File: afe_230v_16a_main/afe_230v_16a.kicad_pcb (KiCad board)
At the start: 2 copper layers, 146 x 86.4 mm, 69 parts, among them J1 MKDSN 2,5/ 6-5,08, J2 MKDS 1,5/ 6, J5 HBUS16, J6 pinheader_2x6_socket, J9 Conn_01x04_STlink_pinheader, U10 BlackPill_F4_SWI, U2 AD8538, U3 AD8538_dnp, U4 AQH3223A, U5 ACS711xLCTR-25AB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

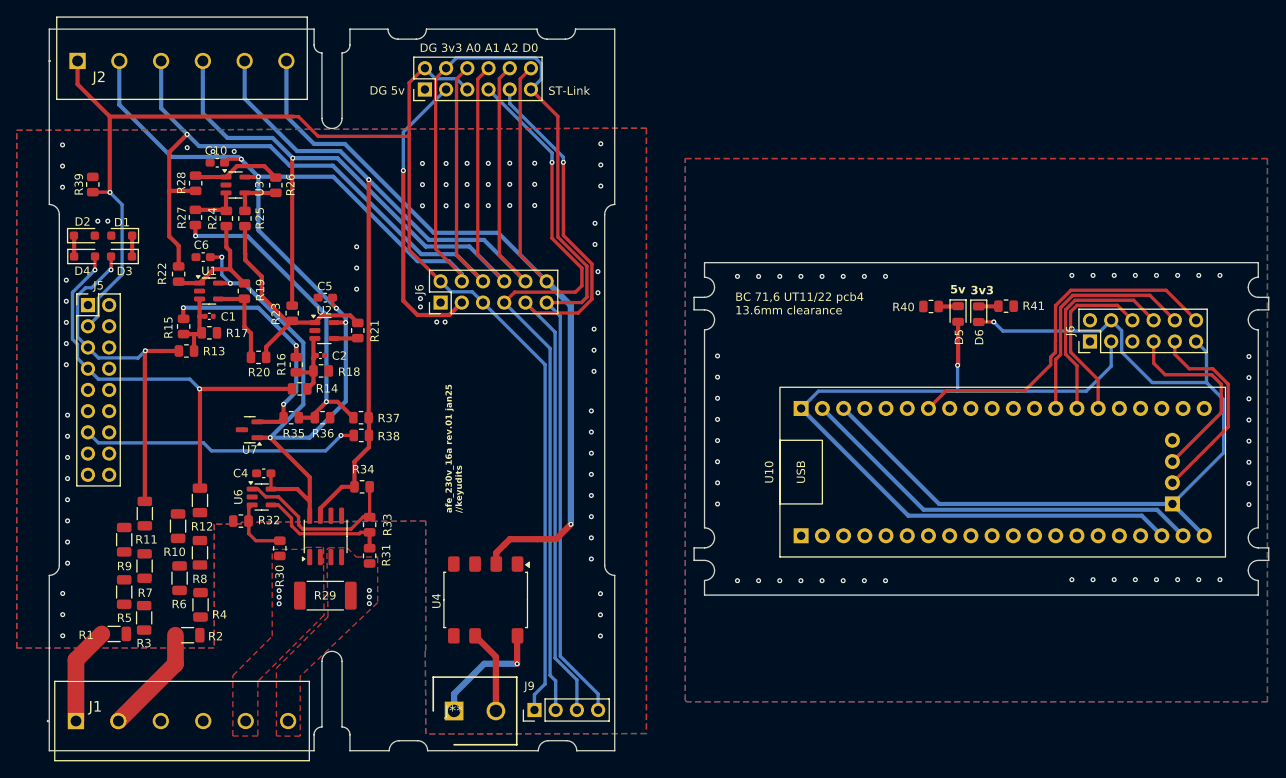
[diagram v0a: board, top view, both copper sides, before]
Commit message: added 15/16 0ohm resistors
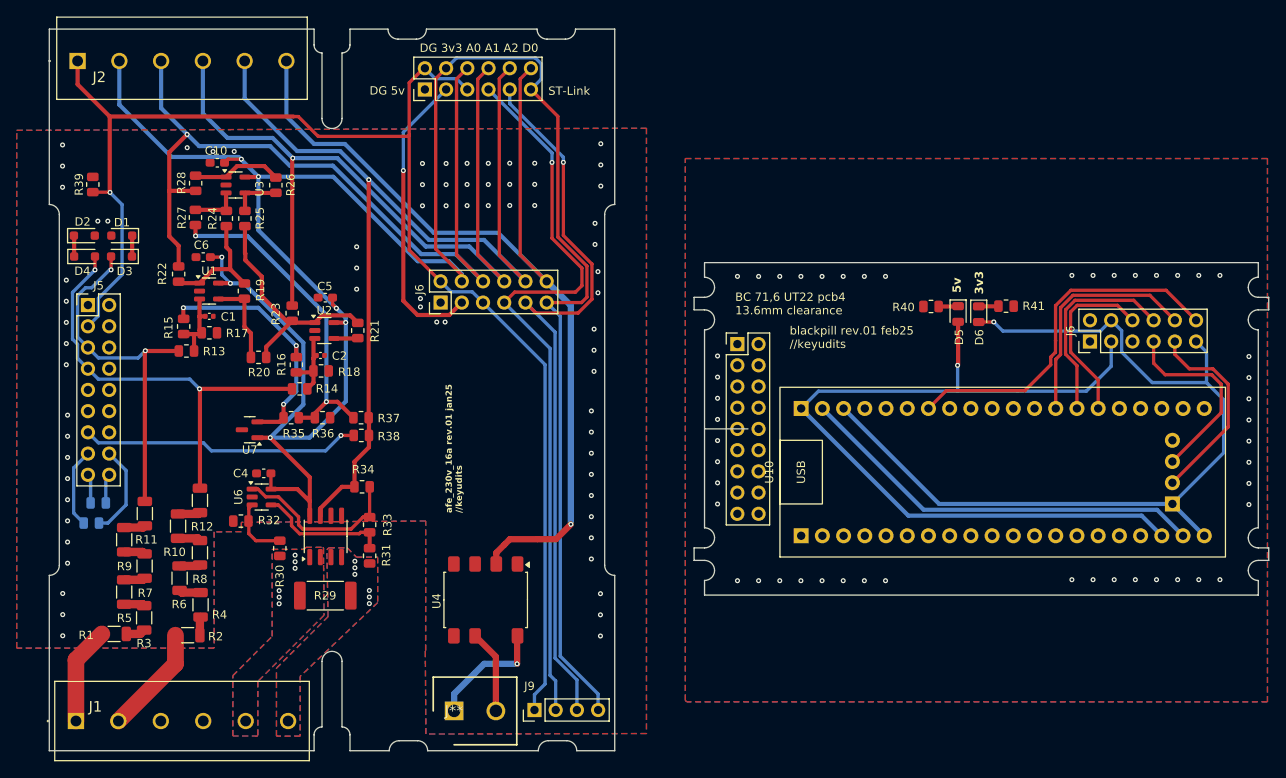
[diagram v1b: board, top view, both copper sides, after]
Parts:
- added J5: HBUS16, Connector_PinHeader_2.54mm:PinHeader_2x09_P2.54mm_Vertical, F.Cu at (200.3, 89.2)
- added R42: 0, Resistor_SMD:R_0805_2012Metric, B.Cu at (123.0, 110.6)
- added R43: 0, Resistor_SMD:R_0805_2012Metric, B.Cu at (123.8, 108.2)
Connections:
- J5 pad 15: unconnected-(J5-Pin_15-Pad15) -> /15a
- J5 pad 16: unconnected-(J5-Pin_16-Pad16) -> /15b
- J5 pad 17: unconnected-(J5-Pin_17-Pad17) -> /16a
- J5 pad 18: unconnected-(J5-Pin_18-Pad18) -> /16b
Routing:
- net /15b: track 0.00 -> 11.1 mm
- net /15a: track 0.00 -> 9.53 mm
- net /16b: track 0.00 -> 4.25 mm
- net /16a: track 0.00 -> 3.79 mm
- net Net-(R10-Pad1): track 0.00 -> 2.73 mm
- net Net-(R10-Pad2): track 0.00 -> 2.68 mm
- net Net-(R4-Pad2): track 0.00 -> 2.62 mm
- net Net-(R11-Pad1): track 0.00 -> 2.55 mm
- net Net-(R7-Pad2): track 0.00 -> 2.53 mm
- net Net-(R5-Pad2): track 0.00 -> 2.52 mm
- net Net-(R6-Pad2): track 0.00 -> 2.49 mm
- net Net-(R3-Pad2): track 0.00 -> 2.46 mm
- net Net-(R1-Pad2): track 0.00 -> 2.33 mm
- net Net-(R2-Pad2): track 0.00 -> 2.21 mm
- net /I_p: vias 3 -> 6
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- added copper zone on B.Cu, net /I_n
- added copper zone on B.Cu, net /I_p
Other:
- outline, holes or cut-outs redrawn
- board text added: "BC 71,6 UT22 pcb4 13.6mm clearance"
- board text added: "blackpill rev.01 feb25 //keyudits"
- board text removed: "BC 71,6 UT11/22 pcb4 13.6mm clearance"

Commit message: gerbers plotted, pcbs on order
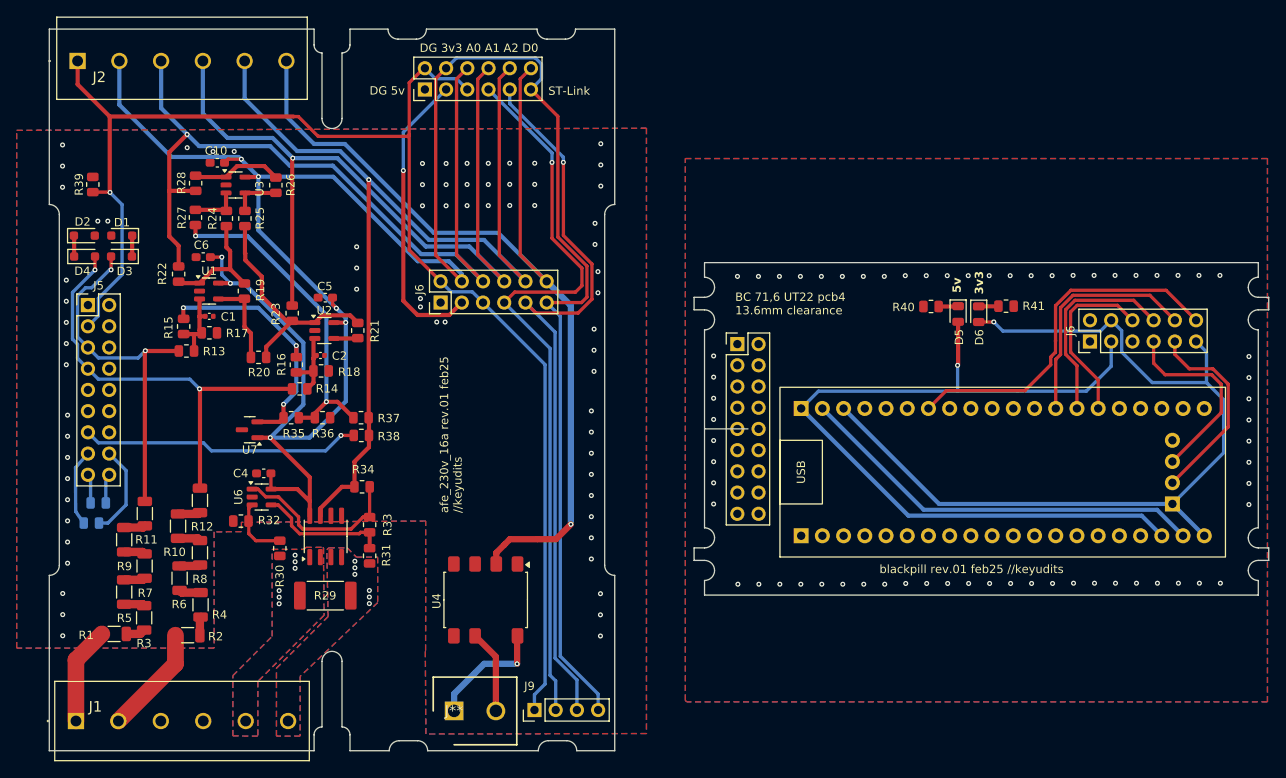
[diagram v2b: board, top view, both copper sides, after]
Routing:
- net Earth: vias 118 -> 134
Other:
- board text added: "JLCJLCJLCJLC"
- board text added: "afe_230v_16a rev.01 feb25 //keyudits"
- board text removed: "afe_230v_16a rev.01 jan25 //keyudits"

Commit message: changed r20 net
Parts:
- added REF**: PinHeader_1x02_P2.54mm_Vertical, Connector_PinHeader_2.54mm:PinHeader_1x02_P2.54mm_Vertical, F.Cu at (131.6, 95.5)
- moved R20 1.88 mm to (141.4, 91.7)
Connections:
- R20 pad 1: Net-(U1--) -> Net-(R19-Pad1)
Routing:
- net Net-(R19-Pad1): track 14.7 -> 31.3 mm, vias 0 -> 2
- net Net-(U1--): track 10.5 -> 3.12 mm
- net Earth: track 49.5 -> 55.0 mm
- net /V1_sense: track 52.7 -> 57.1 mm
- net /V0_sense: track 43.4 -> 45.7 mm
- net Net-(R20-Pad2): track 28.4 -> 30.0 mm
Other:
- board text added: "V0_sense V1_sense"
- board text added: "afe_230v_16a rev.02 aug25 //keyudits"
- board text removed: "afe_230v_16a rev.01 feb25 //keyudits"

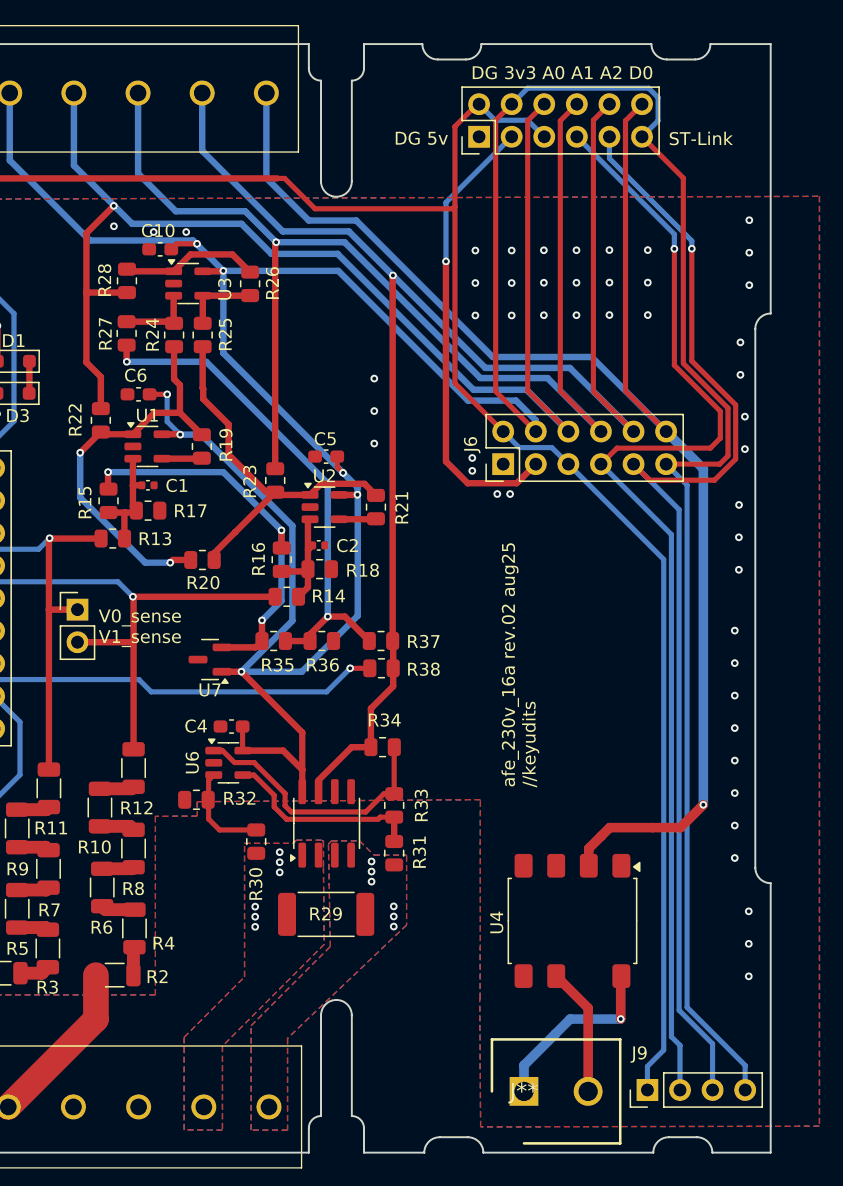
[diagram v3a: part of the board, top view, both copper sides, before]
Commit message: adjusted PCB for rev.2 aug25
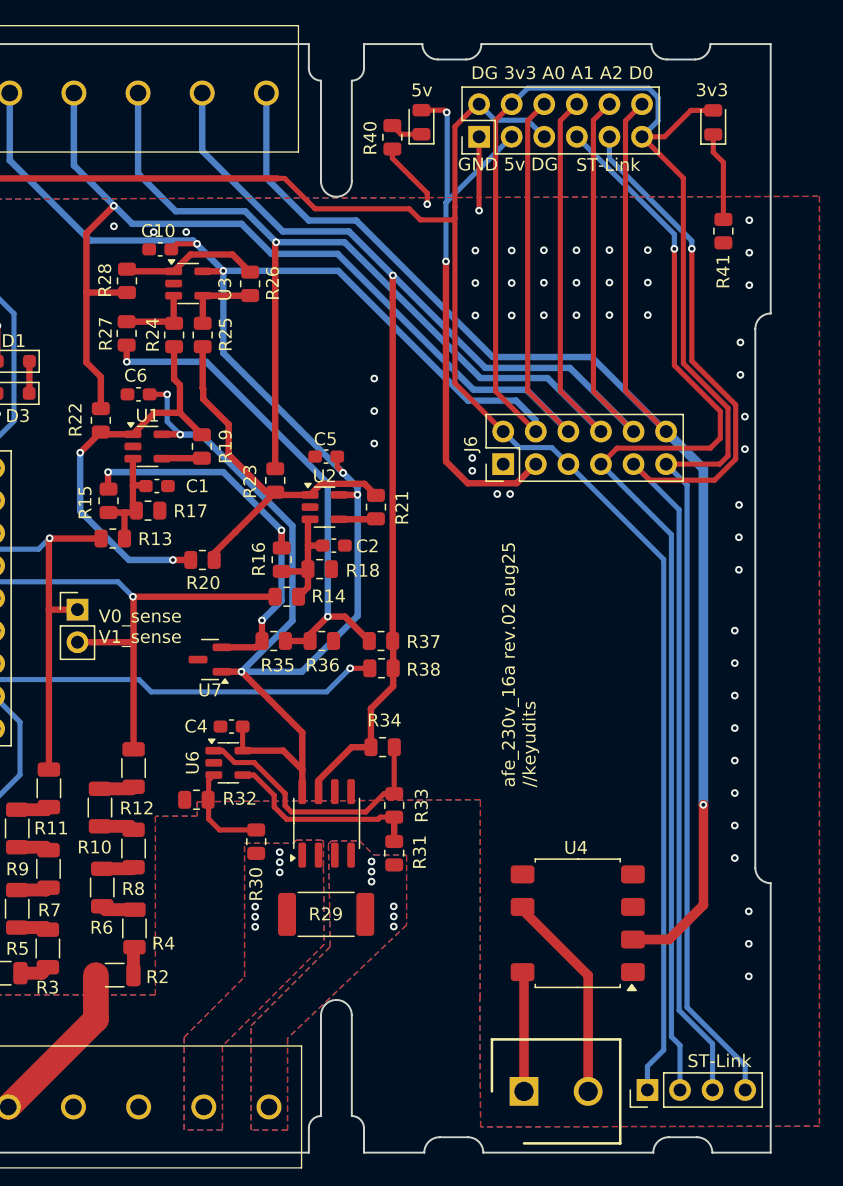
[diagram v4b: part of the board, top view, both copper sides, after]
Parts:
- added 3v3: LED, LED_SMD:LED_0805_2012Metric, F.Cu at (181.2, 57.6)
- added 5v: LED, LED_SMD:LED_0805_2012Metric, F.Cu at (158.4, 57.5)
- added R40: 2.2k, Resistor_SMD:R_0805_2012Metric, F.Cu at (156.2, 58.7)
- added R41: 2.2k, Resistor_SMD:R_0805_2012Metric, F.Cu at (182.0, 66.0)
- C1, C2: footprint Capacitor_SMD:C_0402_1005Metric -> Capacitor_SMD:C_0603_1608Metric_Pad1.08x0.95mm_HandSolder
- moved C2 1.18 mm to (151.6, 90.5)
- moved C1 0.70 mm to (137.8, 85.9)
- moved U4 0.45 mm to (170.6, 120.0), turned to 180 degrees
- turned R19 to 90 degrees
- renumbered J9 to ST-Link
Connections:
- R19 pad 1: Net-(R19-Pad1) -> Net-(U1--)
- R19 pad 2: Net-(U1--) -> Net-(R19-Pad2)
- R20 pad 1: Net-(R19-Pad1) -> Net-(R19-Pad2)
- R21 pad 1: Net-(R20-Pad2) -> Net-(U2--)
- R21 pad 2: Net-(U2--) -> Net-(R20-Pad2)
- R22 pad 1: Net-(R19-Pad1) -> Net-(R19-Pad2)
- R24 pad 1: Net-(R19-Pad1) -> Net-(R19-Pad2)
- U1 pad 1: Net-(R19-Pad1) -> Net-(R19-Pad2)
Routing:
- net Net-(R19-Pad2): track 0.00 -> 31.7 mm, vias 0 -> 2
- net Net-(R19-Pad1): track 31.3 -> 0.00 mm, vias 2 -> 0
- net Earth: track 55.0 -> 66.3 mm, vias 134 -> 136
- net /5v: track 135.9 -> 145.1 mm, vias 2 -> 3
- net Net-(D6-K): track 2.37 -> 9.32 mm
- net /K_o: track 10.0 -> 16.8 mm
- net /3V3: track 388.3 -> 394.7 mm
- net /K_i: track 14.4 -> 9.69 mm, vias 1 -> 0
- net /D0: track 158.5 -> 161.3 mm
- net Net-(D5-K): track 2.35 -> 4.94 mm
- net Net-(U2-+): track 9.04 -> 9.70 mm
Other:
- board text added: "GND 5v DG"
- board text removed: "DG 5v"
